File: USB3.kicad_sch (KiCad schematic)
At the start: 10 parts, among them P1 USB_C_Receptacle, U1 NCP360SNT1G, U6 HD3SS3220IRNHT

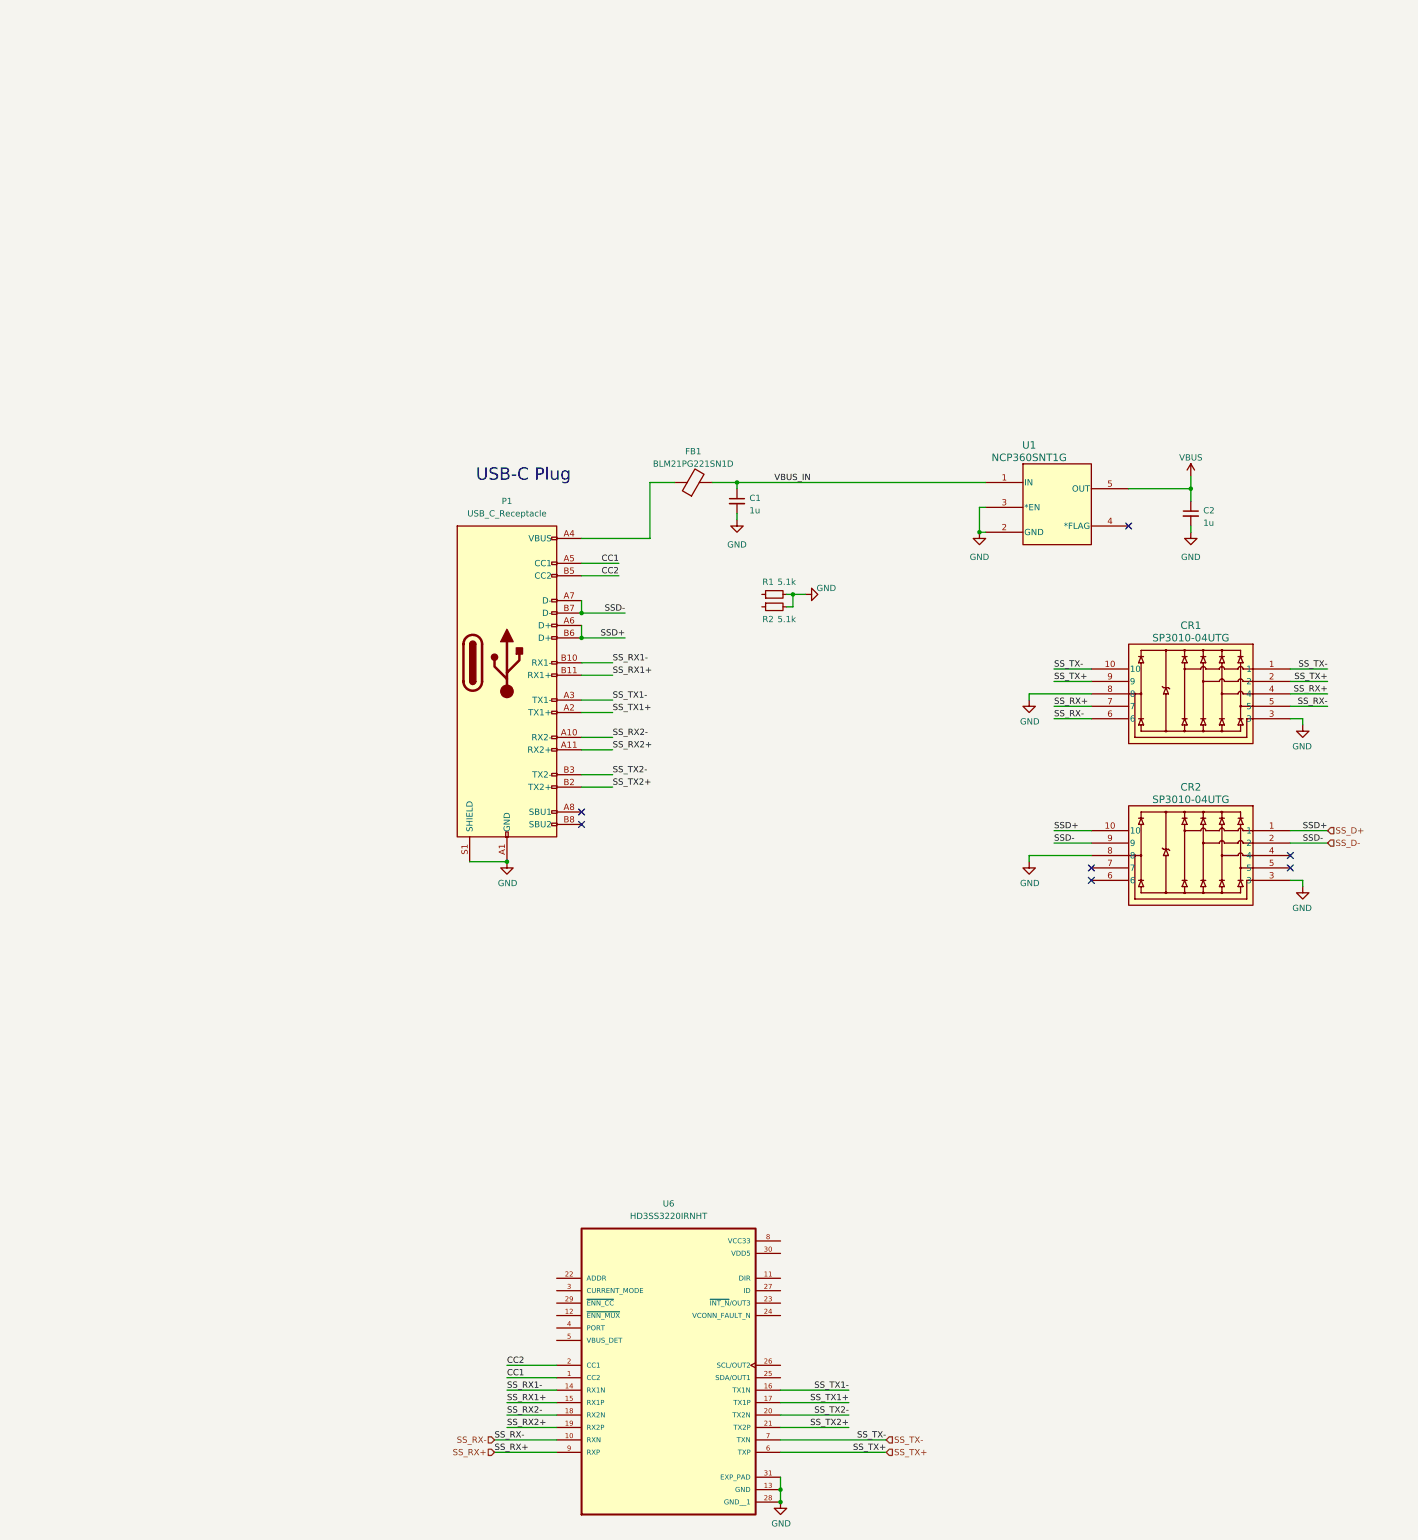
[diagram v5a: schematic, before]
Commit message: change usb c plug
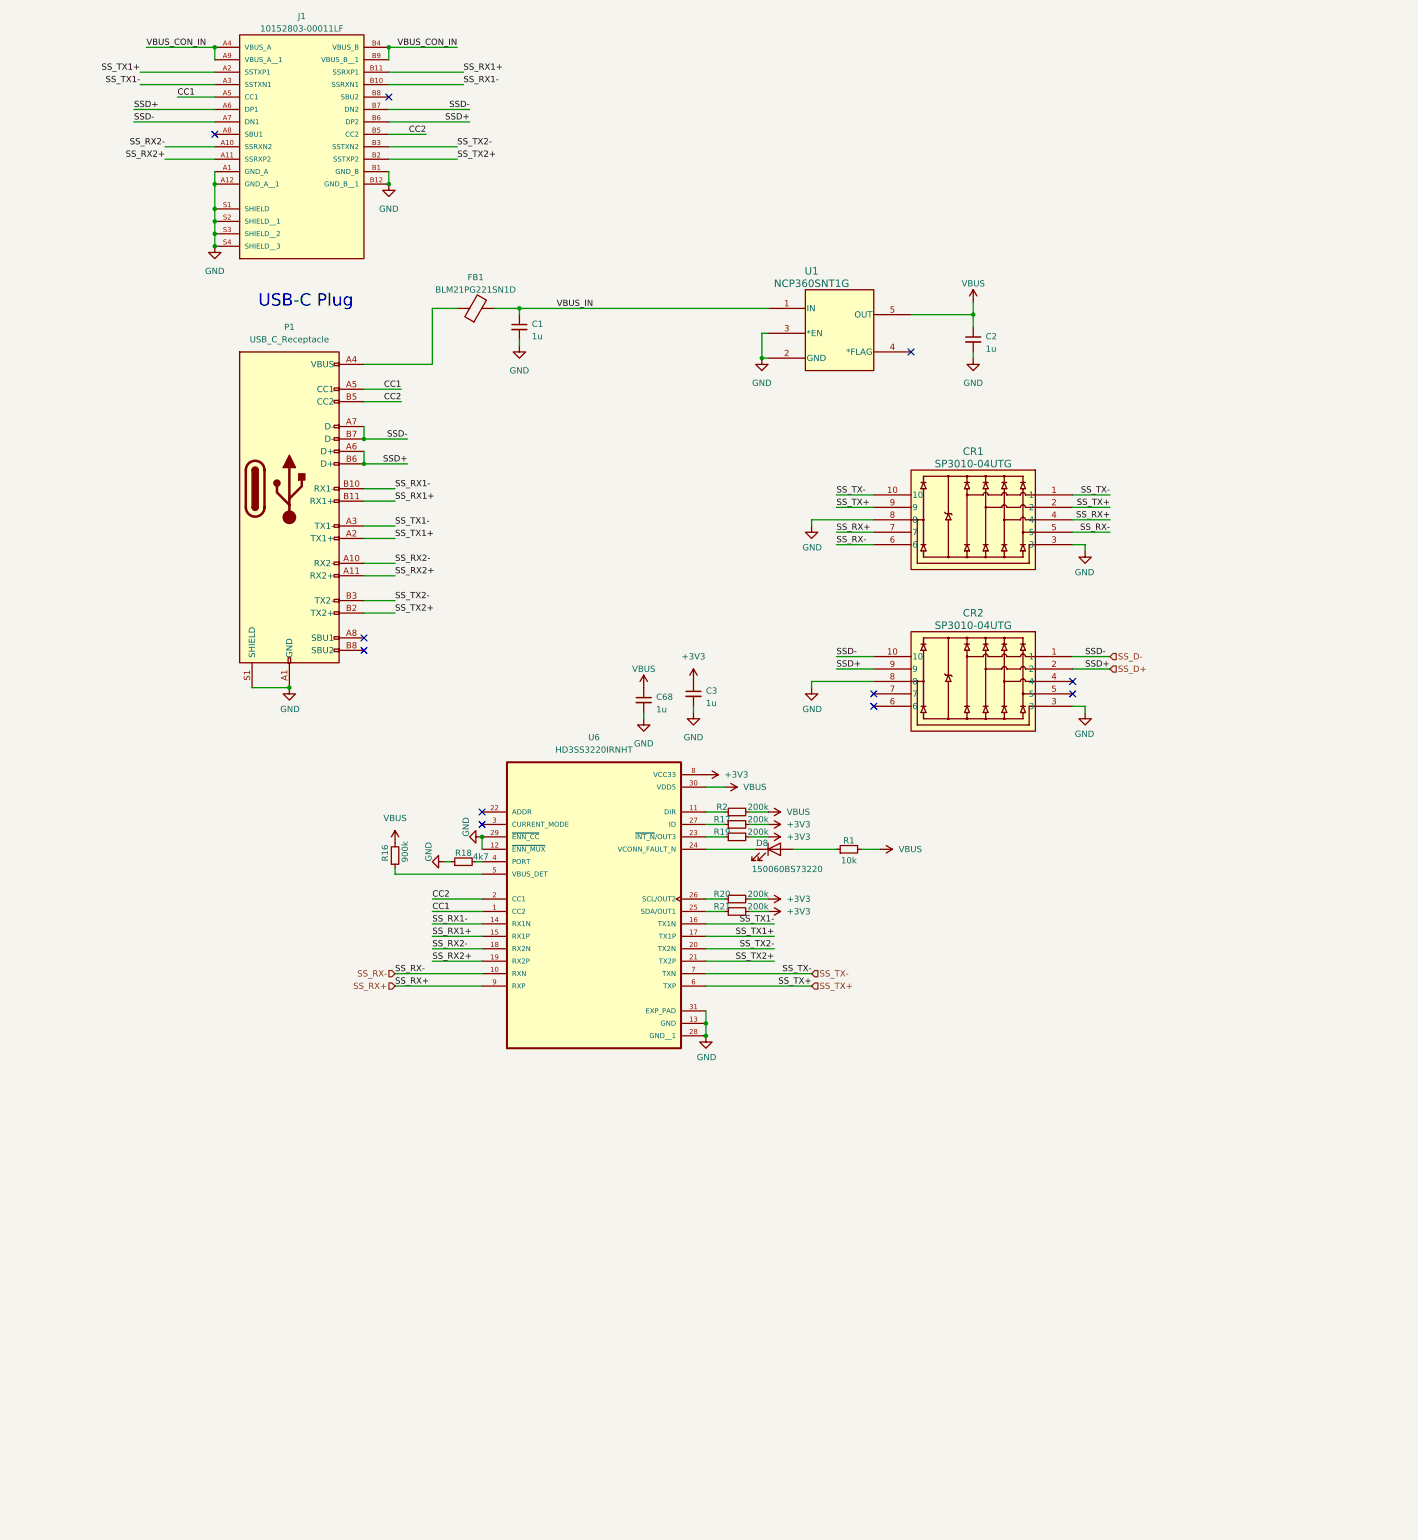
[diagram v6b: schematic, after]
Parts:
- added C3, C68: 1u, Capacitor_SMD:C_0402_1005Metric, symbol Device:C_Small
- added D8: 150060BS73220, LED_SMD:LED_0603_1608Metric_Pad1.05x0.95mm_HandSolder, symbol Device:LED
- added J1: 10152803-00011LF, Snapeda:10152803-00011LF_AMPHENOL_10152803-00011LF, symbol Snapeda:10152803-00011LF
- added R16: 900k, Resistor_SMD:R_0402_1005Metric, symbol Device:R_Small
- added R17, R19, R20, R21: 200k, Resistor_SMD:R_0402_1005Metric, symbol Device:R_Small
- added R18: 4k7, Resistor_SMD:R_0402_1005Metric, symbol Device:R_Small
- R1: value 5.1k -> 10k
- R2: value 5.1k -> 200k
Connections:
- net CC1: now also J1.A5 (CC1)
- net CC2: now also J1.B5 (CC2)
- net GND: now also U6.12 (~{ENN_MUX}), U6.29 (~{ENN_CC}), C3.2, C68.2, J1.A1 (GND_A), J1.A12 (GND_A__1), J1.B1 (GND_B), J1.B12 (GND_B__1), J1.S1 (SHIELD), J1.S2 (SHIELD__1), J1.S3 (SHIELD__2), J1.S4 (SHIELD__3), R18.1; no longer R1.2, R2.2
- net SS_D+: now also CR2.2, CR2.9, J1.A6 (DP1), J1.B6 (DP2); no longer CR2.1, CR2.10
- net SS_D-: now also CR2.1, CR2.10, J1.A7 (DN1), J1.B7 (DN2); no longer CR2.2, CR2.9
- net SS_RX1+: now also J1.B11 (SSRXP1)
- net SS_RX1-: now also J1.B10 (SSRXN1)
- net SS_RX2+: now also J1.A11 (SSRXP2)
- net SS_RX2-: now also J1.A10 (SSRXN2)
- net SS_TX1+: now also J1.A2 (SSTXP1)
- net SS_TX1-: now also J1.A3 (SSTXN1)
- net SS_TX2+: now also J1.B2 (SSTXP2)
- net SS_TX2-: now also J1.B3 (SSTXN2)
- net VBUS: now also R1.2, R2.2, U6.30 (VDD5), C68.1, R16.2
- net at U6.11 (DIR): now also R2.1
- net at U6.23 (~{INT_N}/OUT3): now also R19.1
- net at U6.24 (VCONN_FAULT_N): now also D8.1 (K)
- net at U6.25 (SDA/OUT1): now also R21.1
- net at U6.26 (SCL/OUT2): now also R20.1
- net at U6.27 (ID): now also R17.1
- net at U6.4 (PORT): now also R18.2
- net at U6.5 (VBUS_DET): now also R16.1
- net +3V3: now reaches U6.8 (VCC33)
- net +3V3: now also C3.1, R17.2, R19.2, R20.2, R21.2
- net at R1.1: now also D8.2 (A)
- new net VBUS_CON_IN: J1.A4 (VBUS_A), J1.A9 (VBUS_A__1), J1.B4 (VBUS_B), J1.B9 (VBUS_B__1)
- no-connect marks 7 -> 11
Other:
- moved on the sheet: C1, C2, CR1, CR2, FB1, P1, U1, U6

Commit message: implement USB3.0 active redriver and fix DRC errors
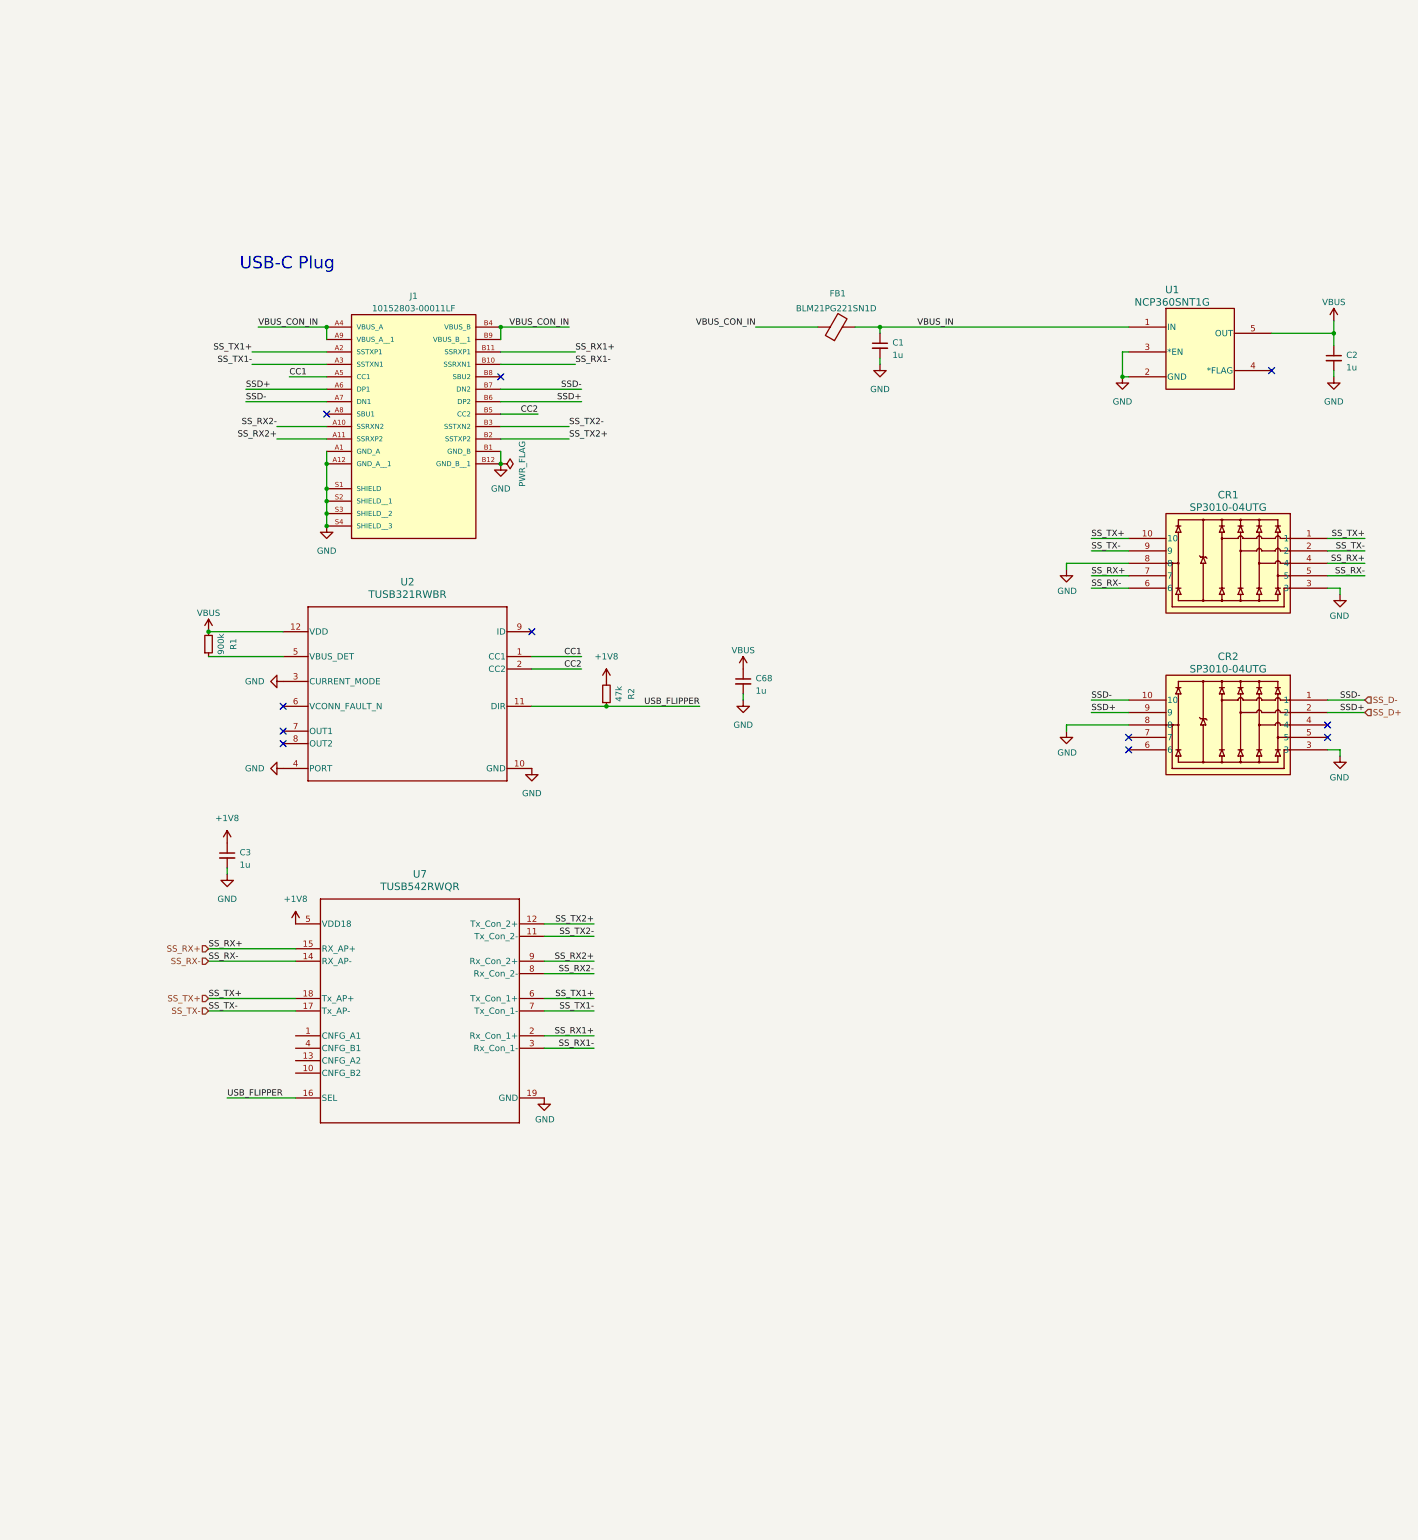
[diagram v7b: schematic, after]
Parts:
- removed D8: 150060BS73220, LED_SMD:LED_0603_1608Metric_Pad1.05x0.95mm_HandSolder, symbol Device:LED
- removed P1: USB_C_Receptacle, Snapeda:USB4056-03-A_REVA2_GCT_USB4056-03-A_REVA2, symbol Connector:USB_C_Receptacle
- removed R16: 900k, Resistor_SMD:R_0402_1005Metric, symbol Device:R_Small
- removed R17, R19, R20, R21: 200k, Resistor_SMD:R_0402_1005Metric, symbol Device:R_Small
- removed R18: 4k7, Resistor_SMD:R_0402_1005Metric, symbol Device:R_Small
- removed U6: HD3SS3220IRNHT, Snapeda:HD3SS3220IRNHT_QFN40P450X250X80-31N120X320, symbol Snapeda:HD3SS3220IRNHT
- added U2: TUSB321RWBR, Snapeda:RWB0012A, symbol Snapeda:TUSB321RWBR
- added U7: TUSB542RWQR, Snapeda:RWQ0018A, symbol Snapeda:TUSB542RWQR
- R1: value 10k -> 900k
- R2: value 200k -> 47k
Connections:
- net CC1: now also U2.1 (CC1)
- net CC2: now also U2.2 (CC2)
- net GND: now also U2.10 (GND), U2.3 (CURRENT_MODE), U2.4 (PORT), U7.19 (GND)
- net SS_RX+: now also U7.15 (RX_AP+)
- net SS_RX-: now also U7.14 (RX_AP-)
- net SS_RX1+: now also U7.2 (Rx_Con_1+)
- net SS_RX1-: now also U7.3 (Rx_Con_1-)
- net SS_RX2+: now also U7.9 (Rx_Con_2+)
- net SS_RX2-: now also U7.8 (Rx_Con_2-)
- net SS_TX+: now also CR1.1, CR1.10, U7.18 (Tx_AP+); no longer CR1.2, CR1.9
- net SS_TX-: now also CR1.2, CR1.9, U7.17 (Tx_AP-); no longer CR1.1, CR1.10
- net SS_TX1+: now also U7.6 (Tx_Con_1+)
- net SS_TX1-: now also U7.7 (Tx_Con_1-)
- net SS_TX2+: now also U7.12 (Tx_Con_2+)
- net SS_TX2-: now also U7.11 (Tx_Con_2-)
- net VBUS: now also U2.12 (VDD); no longer R2.2
- net VBUS_CON_IN: now also FB1.1
- net USB_FLIPPER: now reaches R2.1
- net USB_FLIPPER: now also U2.11 (DIR), U7.16 (SEL)
- net at R1.1: now also U2.5 (VBUS_DET)
- net +3V3 renamed +1V8
- net +1V8: now also R2.2, U7.5 (VDD18)
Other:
- moved on the sheet: C1, C2, C3, C68, CR1, CR2, FB1, J1, U1

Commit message: add AC caps for redriver; fix ERC and DRC errors
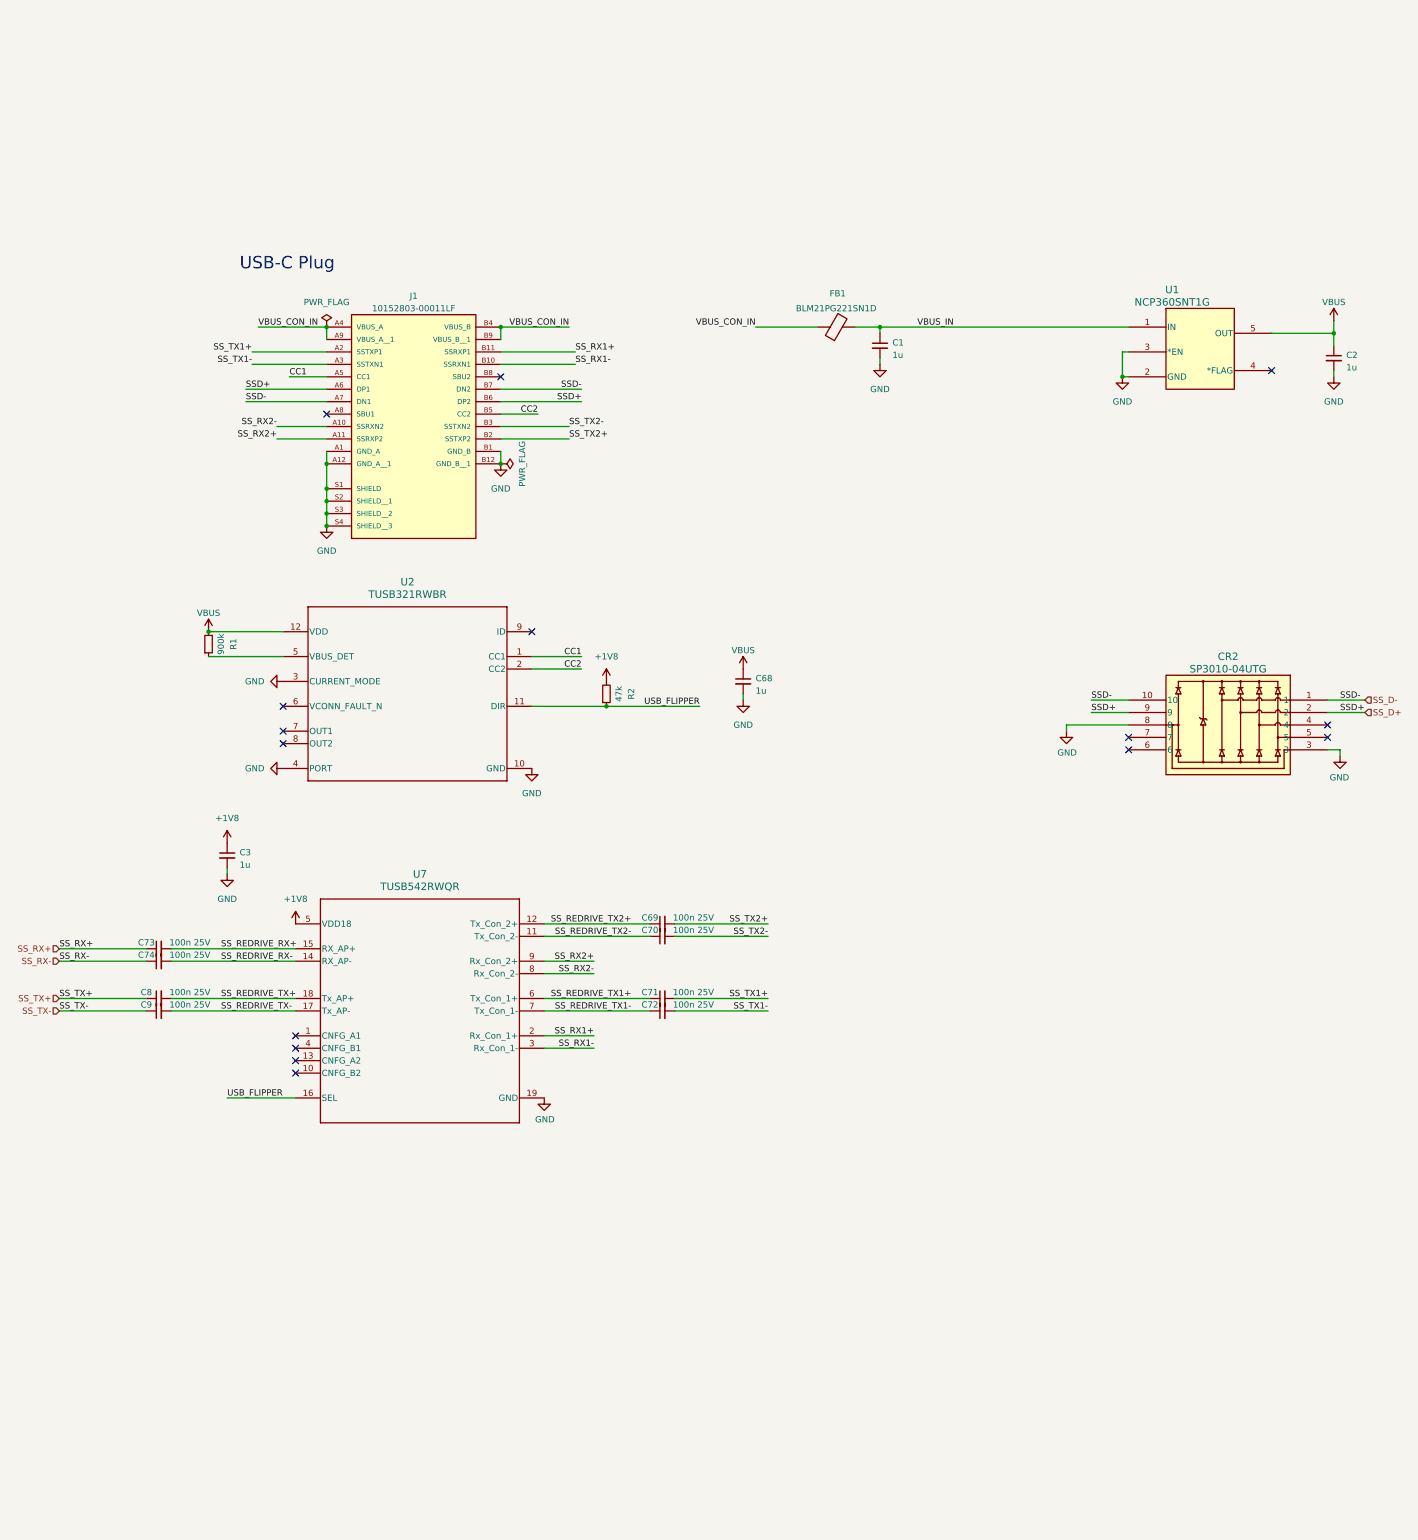
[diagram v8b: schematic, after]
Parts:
- removed CR1: SP3010-04UTG, SP3010:UDFEN-10_MO229_LTF, symbol SP3010-04UTG:SP3010-04UTG
- added C69, C70, C71, C72, C73, C74, C8, C9: 100n 25V, Capacitor_SMD:C_0402_1005Metric, symbol Device:C_Small
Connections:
- net SS_RX+: now also C73.1; no longer U7.15 (RX_AP+)
- net SS_RX-: now also C74.1; no longer U7.14 (RX_AP-)
- net SS_TX+: now also C8.1; no longer U7.18 (Tx_AP+)
- net SS_TX-: now also C9.1; no longer U7.17 (Tx_AP-)
- net SS_TX1+: now also C71.2; no longer U7.6 (Tx_Con_1+)
- net SS_TX1-: now also C72.2; no longer U7.7 (Tx_Con_1-)
- net SS_TX2+: now also C69.2; no longer U7.12 (Tx_Con_2+)
- net SS_TX2-: now also C70.2; no longer U7.11 (Tx_Con_2-)
- new net SS_REDRIVE_RX+: C73.2, U7.15 (RX_AP+)
- new net SS_REDRIVE_RX-: C74.2, U7.14 (RX_AP-)
- new net SS_REDRIVE_TX+: C8.2, U7.18 (Tx_AP+)
- new net SS_REDRIVE_TX-: C9.2, U7.17 (Tx_AP-)
- new net SS_REDRIVE_TX1+: C71.1, U7.6 (Tx_Con_1+)
- new net SS_REDRIVE_TX1-: C72.1, U7.7 (Tx_Con_1-)
- new net SS_REDRIVE_TX2+: C69.1, U7.12 (Tx_Con_2+)
- new net SS_REDRIVE_TX2-: C70.1, U7.11 (Tx_Con_2-)
- no-connect marks 11 -> 15
